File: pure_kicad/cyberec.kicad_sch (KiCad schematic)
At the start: 30 parts, among them J1 XT60M, J2 XT60M, Q1 Q_NMOS_DGS, Q2 Q_NMOS_DGS, Q3 Q_NMOS_DGS, Q4 Q_NMOS_DGS, U1 BQ25756ERRVR

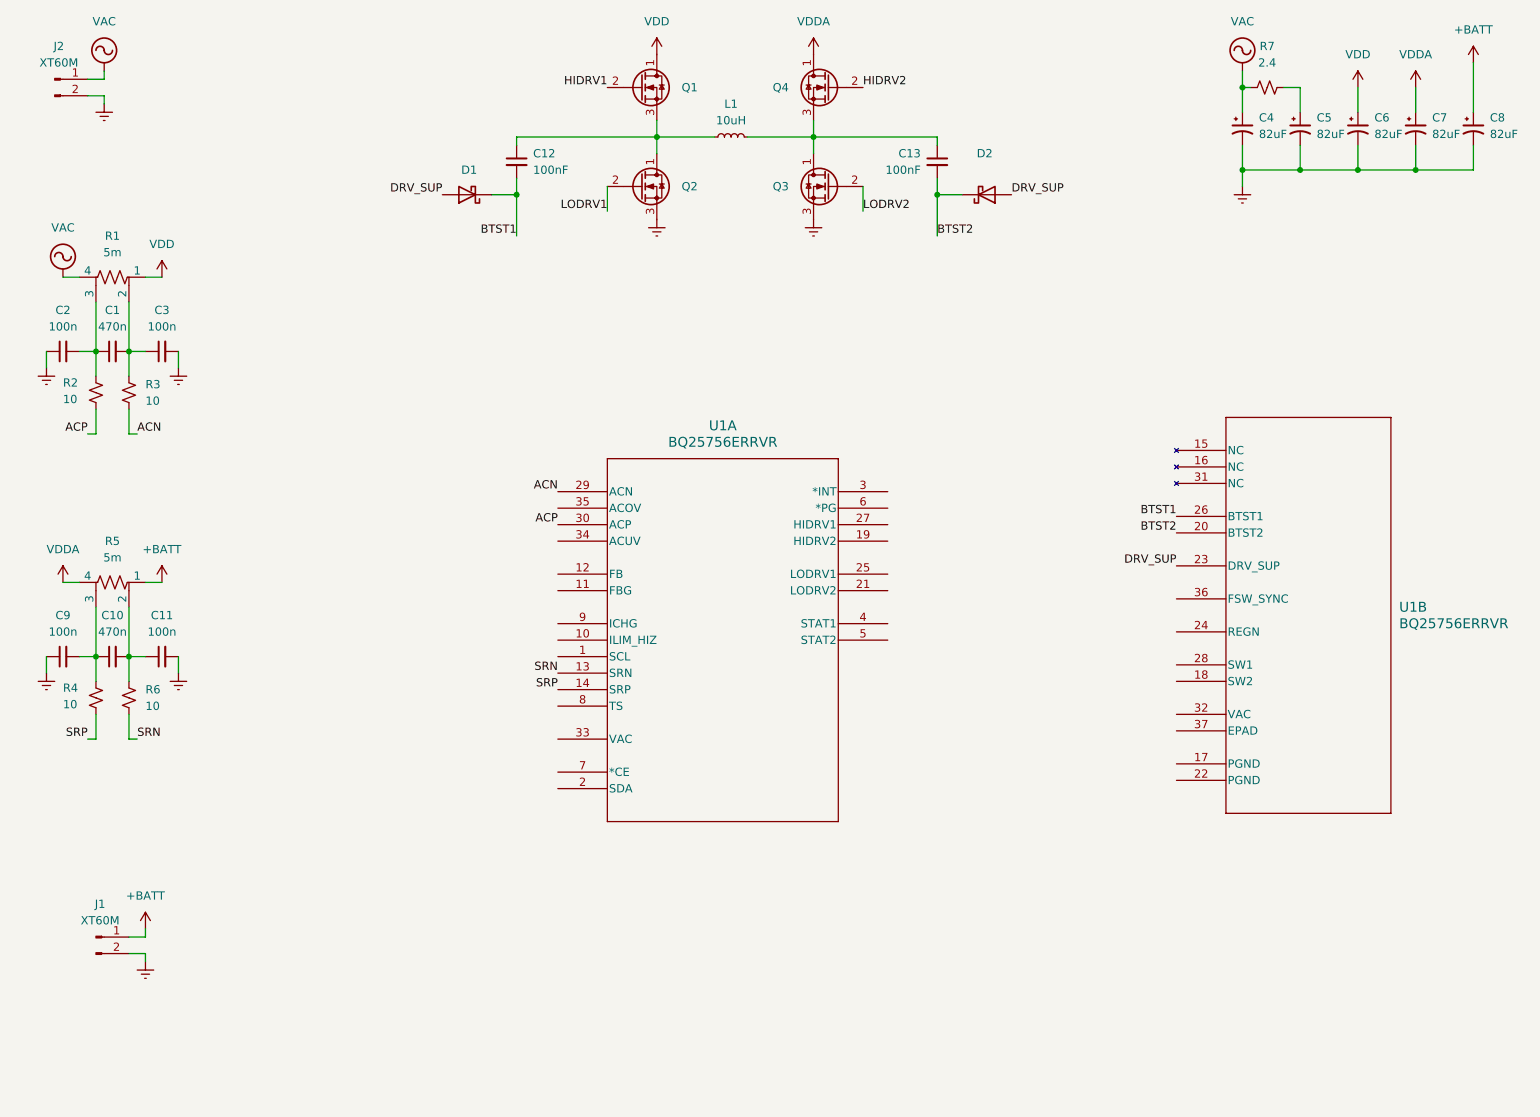
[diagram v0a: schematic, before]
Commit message: Charger Schematic
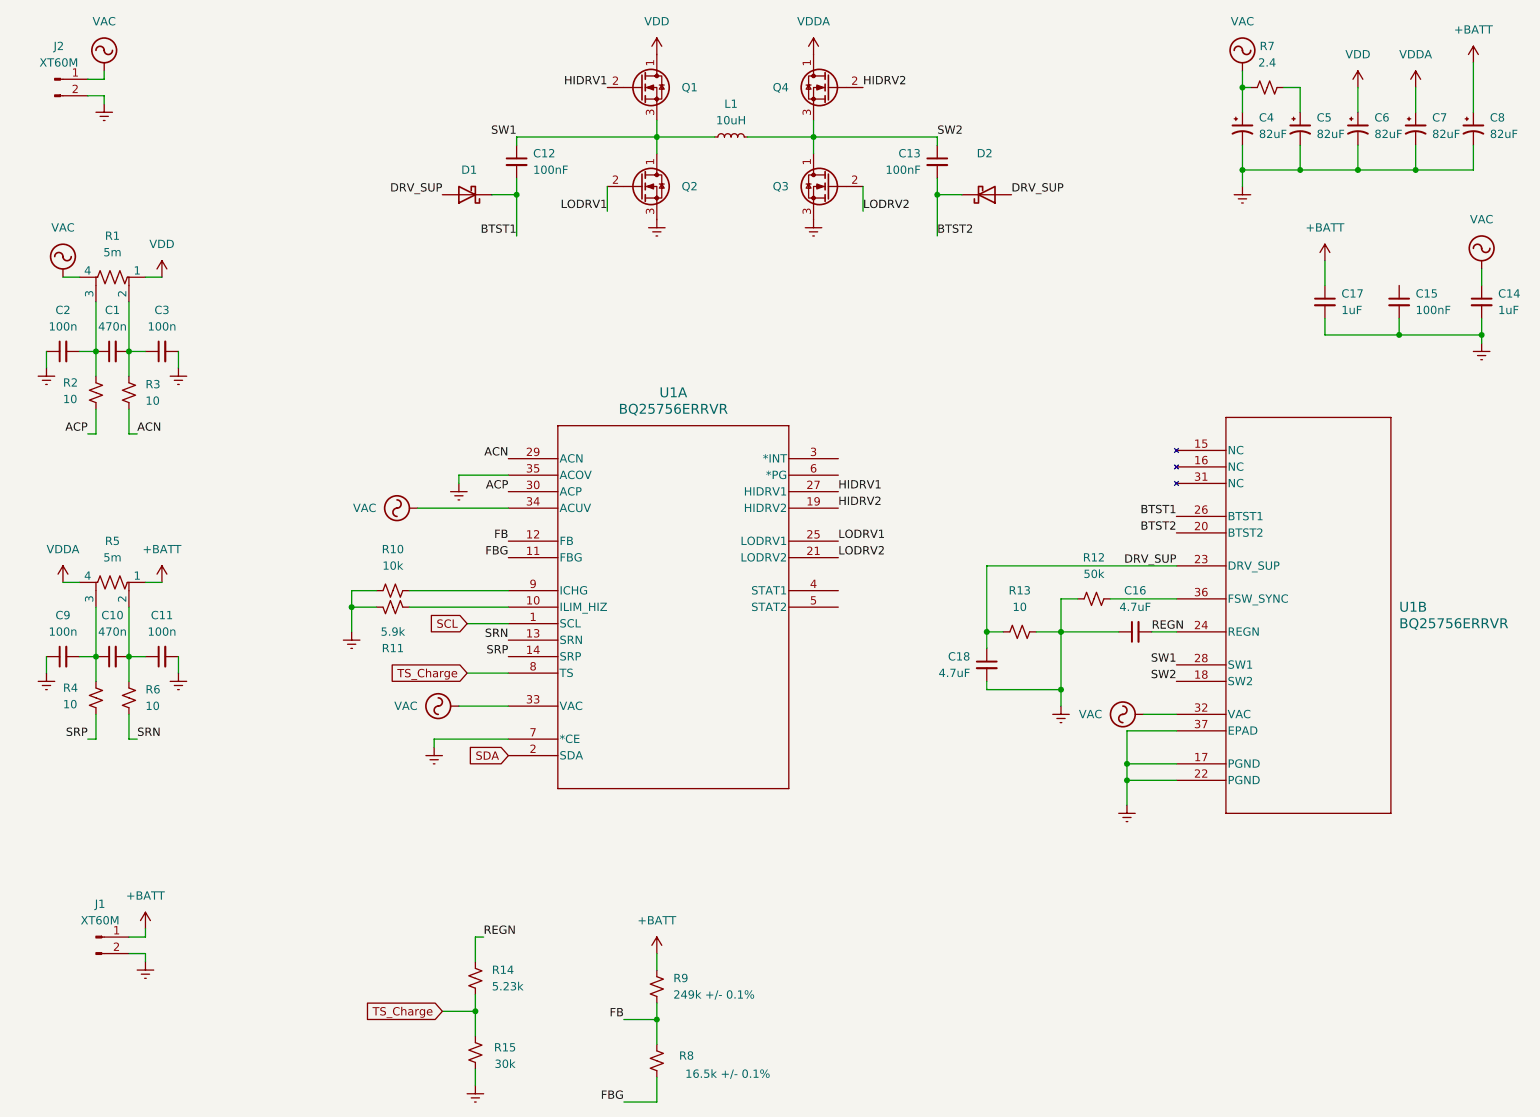
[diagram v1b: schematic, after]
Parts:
- added C14, C17: 1uF, symbol Device:C_Small
- added C15: 100nF, symbol Device:C_Small
- added C16, C18: 4.7uF, Capacitor_SMD:C_0402_1005Metric_Pad0.74x0.62mm_HandSolder, symbol Device:C_Small
- added R10: 10k, Resistor_SMD:R_0402_1005Metric_Pad0.72x0.64mm_HandSolder, symbol Device:R_Small_US
- added R11: 5.9k, Resistor_SMD:R_0402_1005Metric_Pad0.72x0.64mm_HandSolder, symbol Device:R_Small_US
- added R12: 50k, Resistor_SMD:R_0402_1005Metric_Pad0.72x0.64mm_HandSolder, symbol Device:R_Small_US
- added R13: 10, Resistor_SMD:R_0402_1005Metric_Pad0.72x0.64mm_HandSolder, symbol Device:R_Small_US
- added R14: 5.23k, Resistor_SMD:R_0402_1005Metric_Pad0.72x0.64mm_HandSolder, symbol Device:R_Small_US
- added R15: 30k, Resistor_SMD:R_0402_1005Metric_Pad0.72x0.64mm_HandSolder, symbol Device:R_Small_US
- added R8: 16.5k +/- 0.1%, Resistor_SMD:R_0402_1005Metric_Pad0.72x0.64mm_HandSolder, symbol Device:R_Small_US
- added R9: 249k +/- 0.1%, Resistor_SMD:R_0402_1005Metric_Pad0.72x0.64mm_HandSolder, symbol Device:R_Small_US
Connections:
- net +BATT: now also C17.1, R9.1
- net DRV_SUP: now also C18.1, R13.2
- net Earth: now also U1.17 (PGND), U1.22 (PGND), U1.35 (ACOV), U1.37 (EPAD), U1.7 (*CE), C14.2, C15.2, C16.1, C17.2, C18.2, R10.2, R11.2, R12.2, R13.1, R15.2
- net HIDRV1: now also U1.27 (HIDRV1)
- net HIDRV2: now also U1.19 (HIDRV2)
- net LODRV1: now also U1.25 (LODRV1)
- net LODRV2: now also U1.21 (LODRV2)
- net VAC: now also U1.32 (VAC), U1.33 (VAC), U1.34 (ACUV), C14.1
- net SW1: now reaches C12.1, L1.1, Q1.3 (S), Q2.1 (D)
- net SW1: now also U1.28 (SW1)
- net SW2: now reaches C13.1, L1.2, Q3.1 (D), Q4.3 (S)
- net SW2: now also U1.18 (SW2)
- net SCL: now reaches U1.1 (SCL)
- net at U1.10 (ILIM_HIZ): now also R11.1
- net FBG: now reaches U1.11 (FBG)
- net FBG: now also R8.2
- net FB: now reaches U1.12 (FB)
- net FB: now also R8.1, R9.2
- net SDA: now reaches U1.2 (SDA)
- net TS_Charge: now reaches U1.8 (TS)
- net TS_Charge: now also R14.2, R15.1
- net at U1.9 (ICHG): now also R10.1
- net REGN: now reaches U1.24 (REGN)
- net REGN: now also C16.2, R14.1
- net at U1.36 (FSW_SYNC): now also R12.1
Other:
- moved on the sheet: U1A

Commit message: Add battery monitor schematic
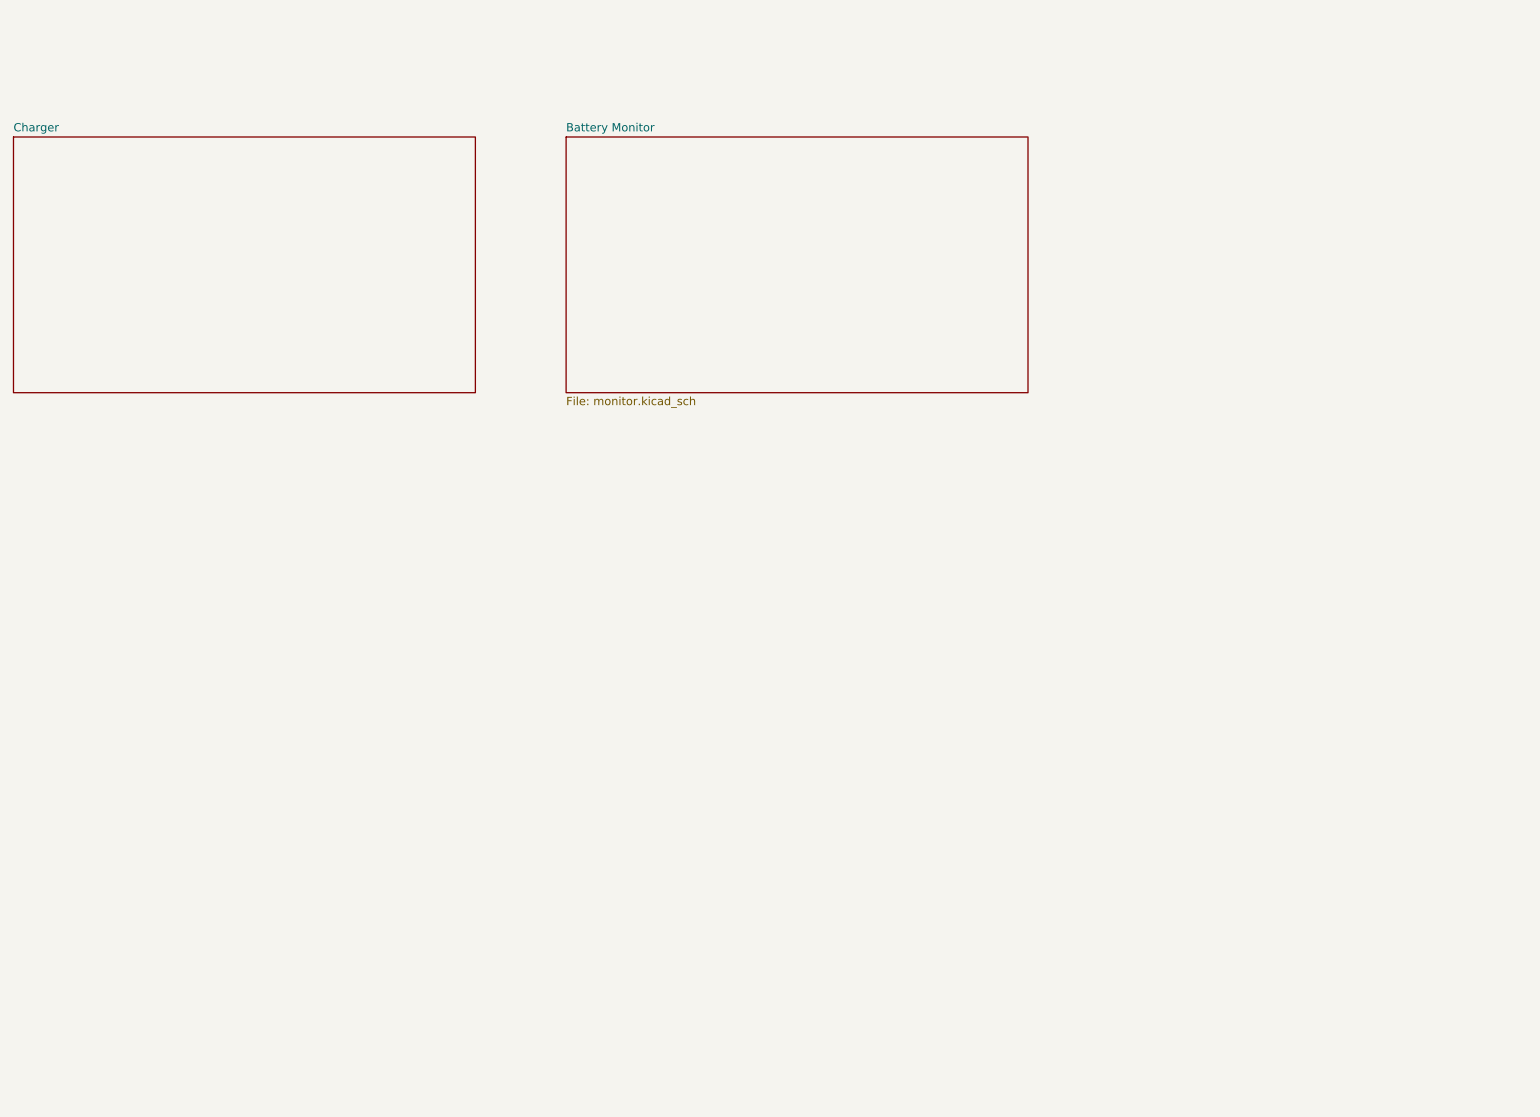
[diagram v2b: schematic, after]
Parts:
- removed C1, C10: 470n, Capacitor_SMD:C_0402_1005Metric_Pad0.74x0.62mm_HandSolder, symbol Device:C_Small
- removed C11, C2, C3, C9: 100n, Capacitor_SMD:C_0402_1005Metric_Pad0.74x0.62mm_HandSolder, symbol Device:C_Small
- removed C12, C13, C15: 100nF, symbol Device:C_Small
- removed C14, C17: 1uF, symbol Device:C_Small
- removed C16, C18: 4.7uF, Capacitor_SMD:C_0402_1005Metric_Pad0.74x0.62mm_HandSolder, symbol Device:C_Small
- removed C4, C5, C6, C7, C8: 82uF, symbol Device:C_Polarized_Small_US
- removed D1, D2: D_Schottky, symbol Device:D_Schottky
- removed J1, J2: XT60M, Connector_AMASS:AMASS_XT60-M_1x02_P7.20mm_Vertical, symbol Connector:Conn_01x02_Pin
- removed L1: 10uH, symbol Device:L_Small
- removed Q1, Q2, Q3, Q4: Q_NMOS_DGS, symbol Transistor_FET:Q_NMOS_DGS
- removed R1, R5: 5m, symbol Device:R_Shunt_US
- removed R10: 10k, Resistor_SMD:R_0402_1005Metric_Pad0.72x0.64mm_HandSolder, symbol Device:R_Small_US
- removed R11: 5.9k, Resistor_SMD:R_0402_1005Metric_Pad0.72x0.64mm_HandSolder, symbol Device:R_Small_US
- removed R12: 50k, Resistor_SMD:R_0402_1005Metric_Pad0.72x0.64mm_HandSolder, symbol Device:R_Small_US
- removed R13, R2, R3, R4, R6: 10, Resistor_SMD:R_0402_1005Metric_Pad0.72x0.64mm_HandSolder, symbol Device:R_Small_US
- removed R14: 5.23k, Resistor_SMD:R_0402_1005Metric_Pad0.72x0.64mm_HandSolder, symbol Device:R_Small_US
- removed R15: 30k, Resistor_SMD:R_0402_1005Metric_Pad0.72x0.64mm_HandSolder, symbol Device:R_Small_US
- removed R7: 2.4, symbol Device:R_Small_US
- removed R8: 16.5k +/- 0.1%, Resistor_SMD:R_0402_1005Metric_Pad0.72x0.64mm_HandSolder, symbol Device:R_Small_US
- removed R9: 249k +/- 0.1%, Resistor_SMD:R_0402_1005Metric_Pad0.72x0.64mm_HandSolder, symbol Device:R_Small_US
- removed U1: BQ25756ERRVR, cyberec:VQFN36_RRV_TEX, symbol cyberec:BQ25756ERRVR
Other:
- added sheet Battery Monitor (monitor.kicad_sch)
- added sheet Charger (charger.kicad_sch)
